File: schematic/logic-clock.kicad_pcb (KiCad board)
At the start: 2 copper layers, 191 x 77.2 mm, 65 parts, among them P11 3-PIN_HEADER, P12 2-PIN_HEADER, P13 3-PIN_HEADER, P14 1-PIN_HEADER, P15 4-PIN_HEADER, P16 4-PIN_HEADER, P17 4-PIN_HEADER, P18 4-PIN_HEADER, P19 4-PIN_HEADER, P20 3-PIN_HEADER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

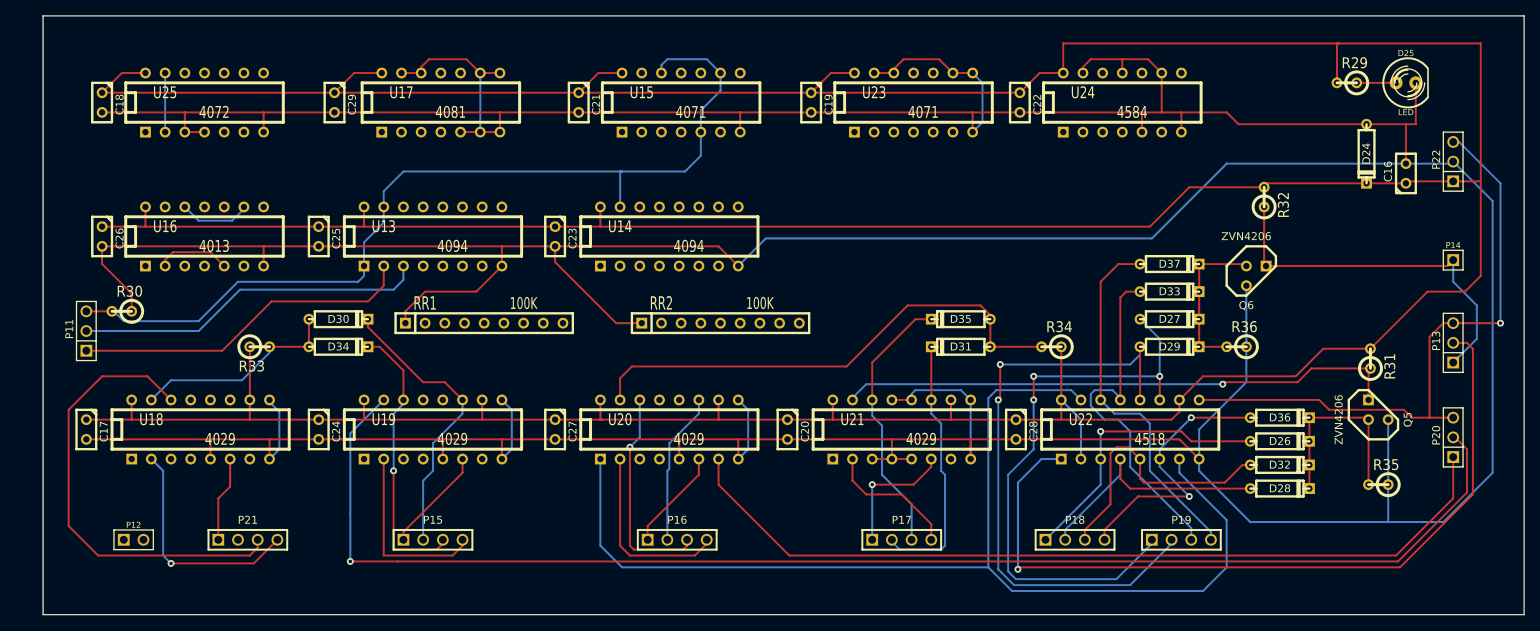
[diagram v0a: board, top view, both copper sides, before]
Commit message: autoroute complete
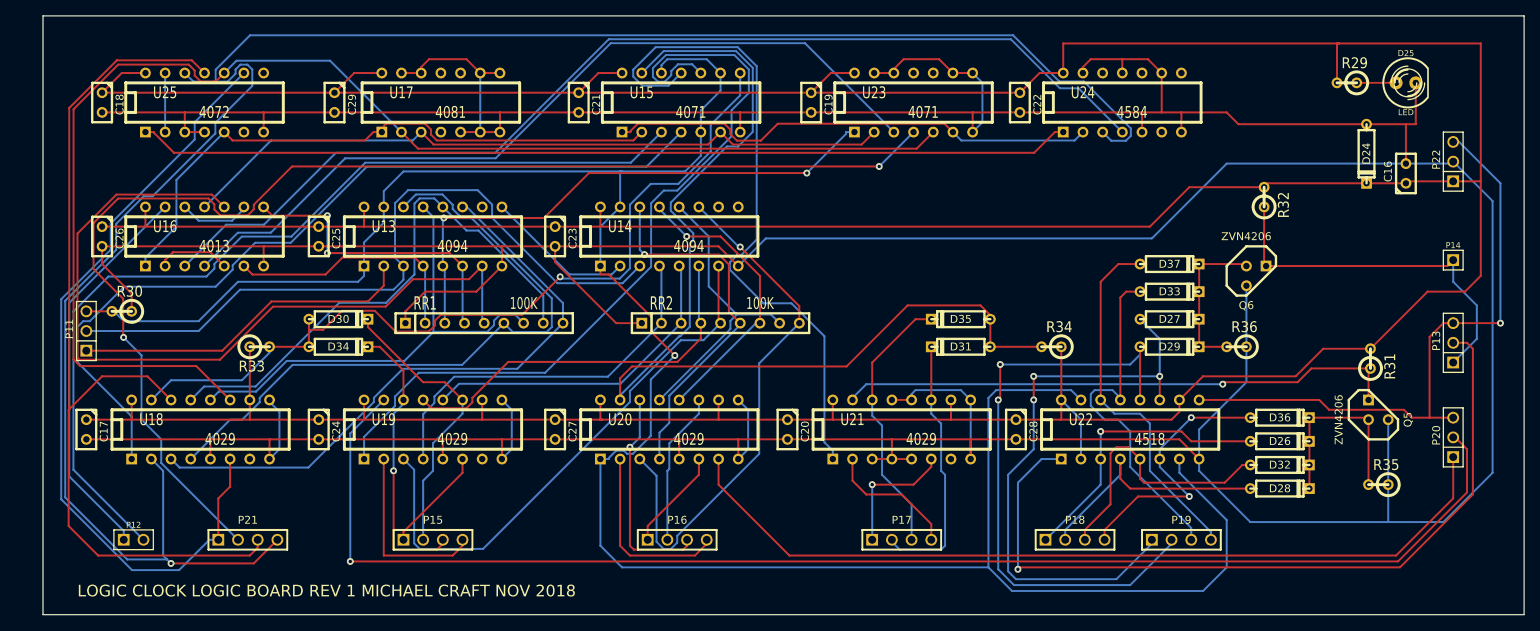
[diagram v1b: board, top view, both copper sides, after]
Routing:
- net /comparator-board/5D: track 29.5 -> 254.1 mm
- net N-00000222: track 0.00 -> 175.9 mm
- net /comparator-board/5B: track 0.00 -> 161.7 mm, vias 0 -> 2
- net N-00000223: track 0.00 -> 138.0 mm
- net N-00000204: track 0.00 -> 120.6 mm
- net /comparator-board/TEN-HOURS: track 0.00 -> 118.9 mm
- net N-00000207: track 0.00 -> 108.5 mm
- net N-00000225: track 0.00 -> 105.6 mm
- net N-00000201: track 0.00 -> 104.5 mm
- net N-00000188: track 0.00 -> 102.5 mm
- net N-00000221: track 0.00 -> 93.0 mm
- net /comparator-board/5A: track 11.0 -> 101.4 mm
- net N-00000200: track 0.00 -> 86.4 mm
- net N-00000187: track 0.00 -> 84.3 mm
- net TEN-MIN_CARRY: track 27.2 -> 107.8 mm, vias 0 -> 1
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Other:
- board text added: "LOGIC CLOCK LOGIC BOARD REV 1 MICHAEL CRAFT NOV 2018"

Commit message: "done"
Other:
- board text added: "+5V"
- board text added: "10-HR"
- board text added: "1HZ"
- board text added: "A"
- board text added: "AM"
- board text added: "BUZZER"
- board text added: "CARRY"
- board text added: "DATA"
- board text added: "FAAST SET"
- board text added: "FAST SET"
- board text added: "HOURS"
- board text added: "MINUTES"
- board text added: "PWR BOARD"
- board text added: "RS232"
- board text added: "SECONDS"
- board text added: "TEN-MINUTES"
- board text added: "TEN-SECONDS"
- board text added: "TENTH-SECONDS"
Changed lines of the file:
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@@
     (links 242)
     (no_connects 0)
-    (area 43.637999 69.037999 234.746001 146.354001)
+    (area 42.978858 69.037999 239.421143 146.354001)
     (thickness 1.6)
-    (drawings 5)
+    (drawings 29)
     (tracks 981)
     (zones 0)
@@
     (15 F.Cu signal)
     (0 B.Cu signal)
+    (20 B.SilkS user)
     (21 F.SilkS user)
+    (22 B.Mask user)
     (23 F.Mask user)
     (28 Edge.Cuts user)
@@
     (visible_elements FFFFFFBF)
     (pcbplotparams
-      (layerselection 3178497)
+      (layerselection 284196865)
       (usegerberextensions true)
       (excludeedgelayer true)
@@
       (plotinvisibletext false)
       (padsonsilk false)
-      (subtractmaskfromsilk false)
+      (subtractmaskfromsilk true)
       (outputformat 1)
       (mirror false)
-      (drillshape 1)
+      (drillshape 0)
       (scaleselection 1)
-      (outputdirectory ""))
+      (outputdirectory gerbers/))
   )
   (net 0 "")
@@
     )
   )
+  (gr_text RS232 (at 46.736 114.808 90) (layer F.SilkS)
+    (effects (font (size 1.5 1.5) (thickness 0.3)))
+  )
+  (gr_text DATA (at 53.34 112.776) (layer F.SilkS)
+    (effects (font (size 1.5 1.5) (thickness 0.3)))
+  )
+  (gr_text A (at 185.928 134.112) (layer F.SilkS)
+    (effects (font (size 1.5 1.5) (thickness 0.3)))
+  )
+  (gr_text A (at 172.212 134.112) (layer F.SilkS)
+    (effects (font (size 1.5 1.5) (thickness 0.3)))
+  )
+  (gr_text A (at 149.86 134.112) (layer F.SilkS)
+    (effects (font (size 1.5 1.5) (thickness 0.3)))
+  )
+  (gr_text A (at 120.904 134.112) (layer F.SilkS)
+    (effects (font (size 1.5 1.5) (thickness 0.3)))
+  )
+  (gr_text A (at 89.408 134.112) (layer F.SilkS)
+    (effects (font (size 1.5 1.5) (thickness 0.3)))
+  )
+  (gr_text A (at 65.532 134.112) (layer F.SilkS)
+    (effects (font (size 1.5 1.5) (thickness 0.3)))
+  )
+  (gr_text 10-HR (at 57.912 131.064 90) (layer F.SilkS)
+    (effects (font (size 1.5 1.5) (thickness 0.3)))
+  )
+  (gr_text AM (at 53.34 133.604 90) (layer F.SilkS)
+    (effects (font (size 1.5 1.5) (thickness 0.3)))
+  )
+  (gr_text HOURS (at 68.58 139.7) (layer F.SilkS)
+    (effects (font (size 1.5 1.5) (thickness 0.3)))
+  )
+  (gr_text TEN-MINUTES (at 96.52 139.7) (layer F.SilkS)
+    (effects (font (size 1.5 1.5) (thickness 0.3)))
+  )
+  (gr_text MINUTES (at 124.968 139.7) (layer F.SilkS)
+    (effects (font (size 1.5 1.5) (thickness 0.3)))
+  )
+  (gr_text TEN-SECONDS (at 157.48 139.7) (layer F.SilkS)
+    (effects (font (size 1.5 1.5) (thickness 0.3)))
+  )
+  (gr_text SECONDS (at 176.784 139.7) (layer F.SilkS)
+    (effects (font (size 1.5 1.5) (thickness 0.3)))
+  )
+  (gr_text TENTH-SECONDS (at 195.072 139.7) (layer F.SilkS)
+    (effects (font (size 1.5 1.5) (thickness 0.3)))
+  )
+  (gr_text "FAAST SET" (at 232.664 123.952 90) (layer F.SilkS)
+    (effects (font (size 1.5 1.5) (thickness 0.3)))
+  )
+  (gr_text CARRY (at 227.584 128.524) (layer F.SilkS)
+    (effects (font (size 1.5 1.5) (thickness 0.3)))
+  )
+  (gr_text "FAST SET" (at 232.664 110.236 90) (layer F.SilkS)
+    (effects (font (size 1.5 1.5) (thickness 0.3)))
+  )
+  (gr_text 1HZ (at 229.108 114.3) (layer F.SilkS)
+    (effects (font (size 1.5 1.5) (thickness 0.3)))
+  )
+  (gr_text BUZZER (at 232.664 97.536 90) (layer F.SilkS)
+    (effects (font (size 1.5 1.5) (thickness 0.3)))
+  )
+  (gr_text 1HZ (at 229.108 101.092) (layer F.SilkS)
+    (effects (font (size 1.5 1.5) (thickness 0.3)))
+  )
+  (gr_text "PWR BOARD" (at 232.664 85.344 90) (layer F.SilkS)
+    (effects (font (size 1.5 1.5) (thickness 0.3)))
+  )
+  (gr_text +5V (at 229.108 90.932) (layer F.SilkS)
+    (effects (font (size 1.5 1.5) (thickness 0.3)))
+  )
   (gr_text "LOGIC CLOCK LOGIC BOARD REV 1 MICHAEL CRAFT NOV 2018" (at 80.264 143.256) (layer F.SilkS)

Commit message: added drill holes, should be ready for manufacture
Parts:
- added ?: Val**, PIN_ARRAY_1, F.Cu at (148.3, 103.6)
- added ?: Val**, PIN_ARRAY_1, F.Cu at (48.8, 74.2)
- added ?: Val**, PIN_ARRAY_1, F.Cu at (48.8, 141.2)
- added ?: Val**, PIN_ARRAY_1, F.Cu at (229.6, 141.2)
- added ?: Val**, PIN_ARRAY_1, F.Cu at (229.6, 74.2)
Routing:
- net +5V: track 666.8 -> 662.3 mm
- net /comparator-board/5C: track 118.1 -> 117.2 mm
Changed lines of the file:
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@@
     (thickness 1.6)
     (drawings 29)
-    (tracks 981)
+    (tracks 984)
     (zones 0)
-    (modules 65)
+    (modules 70)
     (nets 73)
   )
@@
     (mod_text_size 1 1)
     (mod_text_width 0.15)
-    (pad_size 1.5 1.5)
-    (pad_drill 0.6)
+    (pad_size 5.08 5.08)
+    (pad_drill 3.7973)
     (pad_to_mask_clearance 0)
     (aux_axis_origin 0 0)
@@
     (add_net TEN-MIN_CARRY)
   )
+  (module PIN_ARRAY_1 (layer F.Cu)
+    (at 148.336 103.632)
+    (descr "1 pin")
+    (tags "CONN DEV")
+    (fp_text reference "" (at 0 -1.905) (layer F.SilkS)
+      (effects (font (size 0.762 0.762) (thickness 0.1524)))
+    )
+    (fp_text value Val** (at 0 -1.905) (layer F.SilkS) hide
+      (effects (font (size 0.762 0.762) (thickness 0.1524)))
+    )
+    (fp_line (start 1.27 1.27) (end -1.27 1.27) (layer F.SilkS) (width 0.1524))
+    (fp_line (start -1.27 -1.27) (end 1.27 -1.27) (layer F.SilkS) (width 0.1524))
+    (fp_line (start -1.27 1.27) (end -1.27 -1.27) (layer F.SilkS) (width 0.1524))
+    (fp_line (start 1.27 -1.27) (end 1.27 1.27) (layer F.SilkS) (width 0.1524))
+    (pad 1 thru_hole circle (at 0 0) (size 5.08 5.08) (drill 3.7973)
+      (layers *.Cu *.Mask F.SilkS)
+    )
+    (model pin_array\pin_1.wrl
+      (at (xyz 0 0 0))
+      (scale (xyz 1 1 1))
+      (rotate (xyz 0 0 0))
+    )
+  )
+  (module PIN_ARRAY_1 (layer F.Cu)
+    (at 48.768 74.168)
+    (descr "1 pin")
+    (tags "CONN DEV")
+    (fp_text reference "" (at 0 -1.905) (layer F.SilkS)
+      (effects (font (size 0.762 0.762) (thickness 0.1524)))
+    )
+    (fp_text value Val** (at 0 -1.905) (layer F.SilkS) hide
+      (effects (font (size 0.762 0.762) (thickness 0.1524)))
+    )
+    (fp_line (start 1.27 1.27) (end -1.27 1.27) (layer F.SilkS) (width 0.1524))
+    (fp_line (start -1.27 -1.27) (end 1.27 -1.27) (layer F.SilkS) (width 0.1524))
+    (fp_line (start -1.27 1.27) (end -1.27 -1.27) (layer F.SilkS) (width 0.1524))
+    (fp_line (start 1.27 -1.27) (end 1.27 1.27) (layer F.SilkS) (width 0.1524))
+    (pad 1 thru_hole circle (at 0 0) (size 5.08 5.08) (drill 3.7973)
+      (layers *.Cu *.Mask F.SilkS)
+    )
+    (model pin_array\pin_1.wrl
+      (at (xyz 0 0 0))
+      (scale (xyz 1 1 1))
+      (rotate (xyz 0 0 0))
+    )
+  )
+  (module PIN_ARRAY_1 (layer F.Cu)
+    (at 48.768 141.224)
+    (descr "1 pin")
+    (tags "CONN DEV")
+    (fp_text reference "" (at 0 -1.905) (layer F.SilkS)
+      (effects (font (size 0.762 0.762) (thickness 0.1524)))
+    )
+    (fp_text value Val** (at 0 -1.905) (layer F.SilkS) hide
+      (effects (font (size 0.762 0.762) (thickness 0.1524)))
+    )
+    (fp_line (start 1.27 1.27) (end -1.27 1.27) (layer F.SilkS) (width 0.1524))
+    (fp_line (start -1.27 -1.27) (end 1.27 -1.27) (layer F.SilkS) (width 0.1524))
+    (fp_line (start -1.27 1.27) (end -1.27 -1.27) (layer F.SilkS) (width 0.1524))
+    (fp_line (start 1.27 -1.27) (end 1.27 1.27) (layer F.SilkS) (width 0.1524))
+    (pad 1 thru_hole circle (at 0 0) (size 5.08 5.08) (drill 3.7973)
+      (layers *.Cu *.Mask F.SilkS)
+    )
+    (model pin_array\pin_1.wrl
+      (at (xyz 0 0 0))
+      (scale (xyz 1 1 1))
+      (rotate (xyz 0 0 0))
+    )
+  )
+  (module PIN_ARRAY_1 (layer F.Cu)
+    (at 229.616 141.224)
+    (descr "1 pin")
+    (tags "CONN DEV")
+    (fp_text reference "" (at 0 -1.905) (layer F.SilkS)
+      (effects (font (size 0.762 0.762) (thickness 0.1524)))
+    )
+    (fp_text value Val** (at 0 -1.905) (layer F.SilkS) hide
+      (effects (font (size 0.762 0.762) (thickness 0.1524)))
+    )
+    (fp_line (start 1.27 1.27) (end -1.27 1.27) (layer F.SilkS) (width 0.1524))
+    (fp_line (start -1.27 -1.27) (end 1.27 -1.27) (layer F.SilkS) (width 0.1524))
+    (fp_line (start -1.27 1.27) (end -1.27 -1.27) (layer F.SilkS) (width 0.1524))
+    (fp_line (start 1.27 -1.27) (end 1.27 1.27) (layer F.SilkS) (width 0.1524))
+    (pad 1 thru_hole circle (at 0 0) (size 5.08 5.08) (drill 3.7973)
+      (layers *.Cu *.Mask F.SilkS)
+    )
+    (model pin_array\pin_1.wrl
+      (at (xyz 0 0 0))
+      (scale (xyz 1 1 1))
+      (rotate (xyz 0 0 0))
+    )
+  )
   (module TO92DGS (layer F.Cu)
     (at 215.9 119.888 90)
@@
     )
   )
+  (module PIN_ARRAY_1 (layer F.Cu)
+    (at 229.616 74.168)
+    (descr "1 pin")
+    (tags "CONN DEV")
+    (fp_text reference "" (at 0 -1.905) (layer F.SilkS)
+      (effects (font (size 0.762 0.762) (thickness 0.1524)))
+    )
+    (fp_text value Val** (at 0 -1.905) (layer F.SilkS) hide
+      (effects (font (size 0.762 0.762) (thickness 0.1524)))
+    )
+    (fp_line (start 1.27 1.27) (end -1.27 1.27) (layer F.SilkS) (width 0.1524))
+    (fp_line (start -1.27 -1.27) (end 1.27 -1.27) (layer F.SilkS) (width 0.1524))
+    (fp_line (start -1.27 1.27) (end -1.27 -1.27) (layer F.SilkS) (width 0.1524))
+    (fp_line (start 1.27 -1.27) (end 1.27 1.27) (layer F.SilkS) (width 0.1524))
+    (pad 1 thru_hole circle (at 0 0) (size 5.08 5.08) (drill 3.7973)
+      (layers *.Cu *.Mask F.SilkS)
+    )
+    (model pin_array\pin_1.wrl
+      (at (xyz 0 0 0))
+      (scale (xyz 1 1 1))
+      (rotate (xyz 0 0 0))
+    )
+  )
   (gr_text RS232 (at 46.736 114.808 90) (layer F.SilkS)
     (effects (font (size 1.5 1.5) (thickness 0.3)))
@@
     (effects (font (size 1.5 1.5) (thickness 0.3)))
   )
-  (gr_text "LOGIC CLOCK LOGIC BOARD REV 1 MICHAEL CRAFT NOV 2018" (at 80.264 143.256) (layer F.SilkS)
+  (gr_text "LOGIC CLOCK LOGIC BOARD REV 1 MICHAEL CRAFT NOV 2018" (at 87.884 143.256) (layer F.SilkS)
     (effects (font (size 1.5 1.5) (thickness 0.3)))
   )
@@
   (gr_line (start 234.696 69.088) (end 43.688 69.088) (angle 90) (layer Edge.Cuts) (width 0.1))
   (gr_line (start 234.696 146.304) (end 234.696 69.088) (angle 90) (layer Edge.Cuts) (width 0.1))
+  (segment (start 210.566 72.644) (end 220.98 72.644) (width 0.254) (layer F.Cu) (net 1))
+  (segment (start 229.108 85.344) (end 229.108 90.424) (width 0.254) (layer F.Cu) (net 1))
+  (segment (start 223.774 80.01) (end 229.108 85.344) (width 0.254) (layer F.Cu) (net 1))
+  (segment (start 223.774 75.438) (end 223.774 80.01) (width 0.254) (layer F.Cu) (net 1))
+  (segment (start 220.98 72.644) (end 223.774 75.438) (width 0.254) (layer F.Cu) (net 1))
   (segment (start 115.57 93.726) (end 115.57 96.266) (width 0.254) (layer F.Cu) (net 1))
   (segment (start 177.546 121.158) (end 175.006 118.618) (width 0.254) (layer B.Cu) (net 1))
@@
   (segment (start 214.884 112.014) (end 208.788 112.014) (width 0.254) (layer F.Cu) (net 1))
   (segment (start 222.25 104.648) (end 214.884 112.014) (width 0.254) (layer F.Cu) (net 1))
-  (segment (start 227.076 104.648) (end 222.25 104.648) (width 0.254) (layer F.Cu) (net 1))
-  (segment (start 229.108 102.616) (end 227.076 104.648) (width 0.254) (layer F.Cu) (net 1))
   (segment (start 229.108 90.424) (end 229.108 102.616) (width 0.254) (layer F.Cu) (net 1))
+  (segment (start 229.108 102.616) (end 227.076 104.648) (width 0.254) (layer F.Cu) (net 1))
+  (segment (start 227.076 104.648) (end 222.25 104.648) (width 0.254) (layer F.Cu) (net 1))
   (segment (start 201.676 90.678) (end 201.168 91.186) (width 0.254) (layer F.Cu) (net 1))
   (segment (start 214.376 90.678) (end 201.676 90.678) (width 0.254) (layer F.Cu) (net 1))
@@
   (segment (start 175.26 72.644) (end 175.26 76.454) (width 0.254) (layer F.Cu) (net 1))
   (segment (start 210.566 72.644) (end 175.26 72.644) (width 0.254) (layer F.Cu) (net 1))
-  (segment (start 229.108 72.644) (end 210.82 72.644) (width 0.254) (layer F.Cu) (net 1))
-  (segment (start 229.108 90.424) (end 229.108 72.644) (width 0.254) (layer F.Cu) (net 1))
   (segment (start 210.82 72.644) (end 210.566 72.644) (width 0.254) (layer F.Cu) (net 1))
   (segment (start 109.728 96.266) (end 115.57 96.266) (width 0.254) (layer F.Cu) (net 1))
@@
   (segment (start 54.0809 110.5545) (end 54.0278 110.5014) (width 0.254) (layer F.Cu) (net 11))
   (segment (start 46.99 119.888) (end 47.1801 119.6979) (width 0.254) (layer F.Cu) (net 12))
-  (segment (start 46.99 134.874) (end 46.99 119.888) (width 0.254) (layer F.Cu) (net 12))
-  (segment (start 50.8 138.684) (end 46.99 134.874) (width 0.254) (layer F.Cu) (net 12))
-  (segment (start 70.358 138.684) (end 50.8 138.684) (width 0.254) (layer F.Cu) (net 12))
+  (segment (start 46.99 133.35) (end 46.99 119.888) (width 0.254) (layer F.Cu) (net 12))
+  (segment (start 52.324 138.684) (end 46.99 133.35) (width 0.254) (layer F.Cu) (net 12))
+  (segment (start 70.358 138.684) (end 52.324 138.684) (width 0.254) (layer F.Cu) (net 12))
   (segment (start 71.374 137.668) (end 70.358 138.684) (width 0.254) (layer F.Cu) (net 12))
   (segment (start 71.374 136.652) (end 71.374 137.668) (width 0.254) (layer F.Cu) (net 12))
